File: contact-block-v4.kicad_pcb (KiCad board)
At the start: 2 copper layers, 42.5 x 19.2 mm, 10 parts, among them J1 629105136821, J2 M06SIP, J3 MPT2, U1 PIC16F1459-I_SS

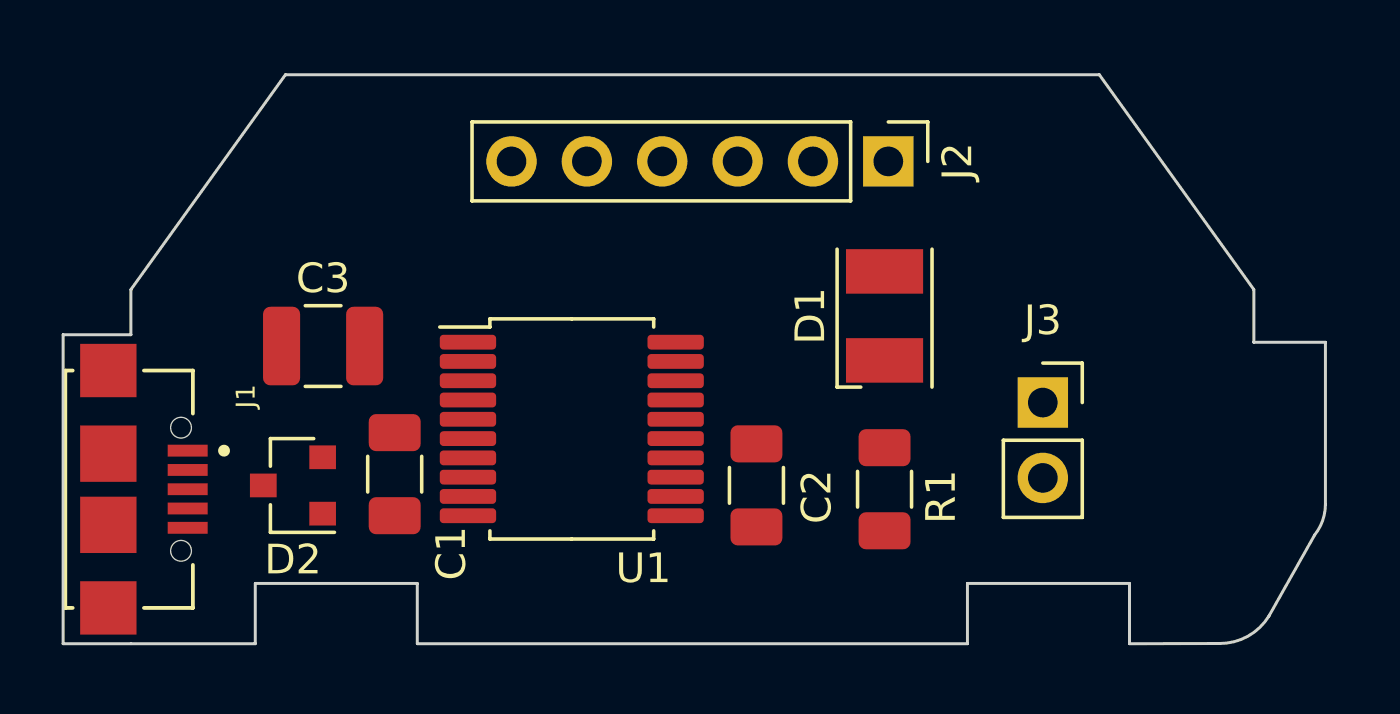
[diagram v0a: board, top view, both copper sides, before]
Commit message: Complete routing and add 3d models
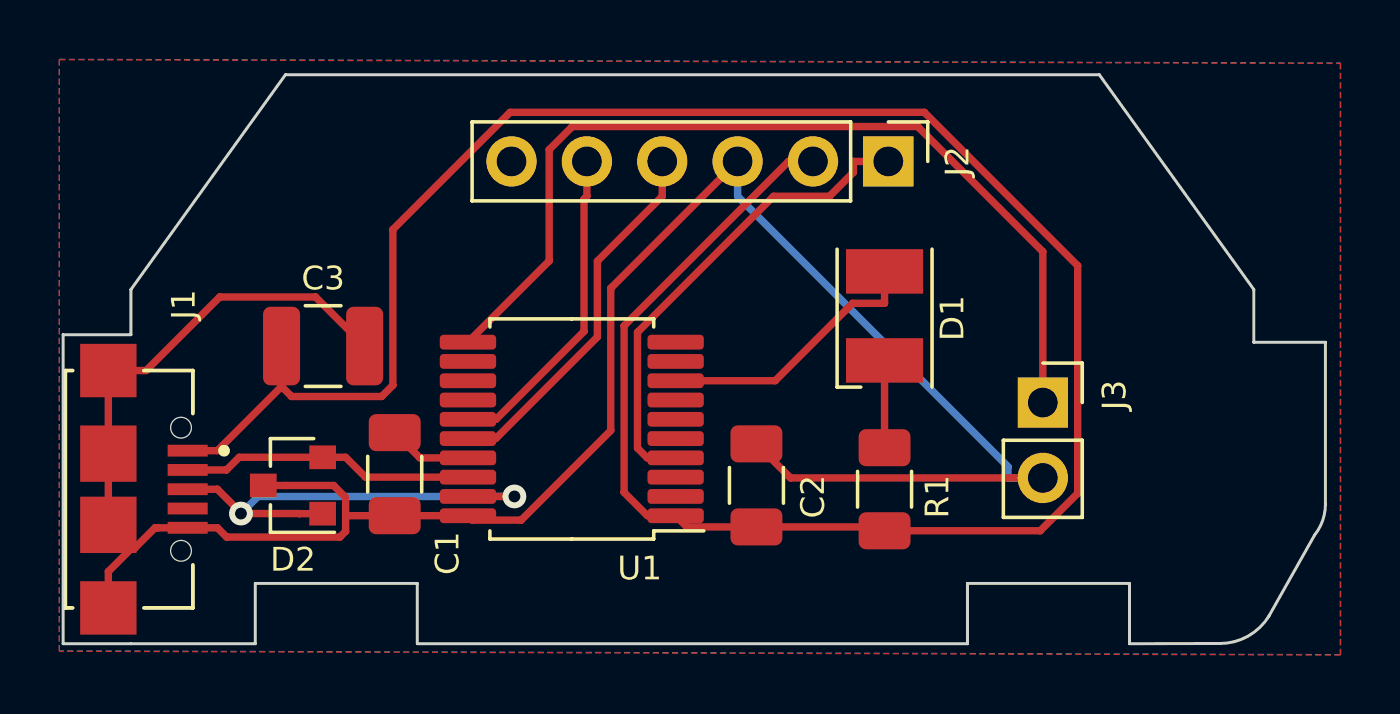
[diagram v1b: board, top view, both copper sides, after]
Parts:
- turned C1 to -90 degrees
- turned R1 to -90 degrees
- turned U1 to 180 degrees
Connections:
- D1 pad 1: (no net) -> Net-(D1-Pad1)
- D1 pad 2: (no net) -> Net-(D1-Pad2)
- J1 pad S1: (no net) -> GND
- J1 pad S2: (no net) -> GND
- J1 pad S3: (no net) -> GND
- J1 pad S4: (no net) -> GND
- R1 pad 1: Net-(D1-PadA) -> Net-(D1-Pad1)
- U1 pad 8: Net-(D1-PadC) -> Net-(D1-Pad2)
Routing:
- net +5V: track 0.00 -> 79.9 mm
- net GND: track 0.00 -> 77.6 mm
- net Net-(J3-Pad1): track 0.00 -> 31.4 mm
- net //MCLR: track 0.00 -> 16.4 mm
- net /D+: track 0.00 -> 15.9 mm, vias 0 -> 2
- net /PGD: track 0.00 -> 12.6 mm
- net /PGC: track 0.00 -> 10.9 mm
- net /D-: track 0.00 -> 9.90 mm
- net Net-(D1-Pad2): track 0.00 -> 9.20 mm
- net Net-(D1-Pad1): track 0.00 -> 2.94 mm
- net Net-(C1-Pad1): track 0.00 -> 2.82 mm
- added copper zone on B.Cu, net GND
- added copper zone on F.Cu, net GND

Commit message: Add doc images and bom
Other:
- board text added: "USB Big Red Button by Tisham Dhar Derived from work by @bikerglen v0.1 29/11/2020 http://whatnick.com OSHW TAPR"
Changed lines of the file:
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@@
     (pad "2" thru_hole oval (at 0 2.54) (size 1.7 1.7) (drill 1) (layers *.Cu *.Mask)
       (net 1 "GND") (pinfunction "1"))
-    (model "${KISYS3DMOD}/Connector_PinSocket_2.54mm.3dshapes/PinSocket_1x02_P2.54mm_Vertical.wrl"
+    (model "${KISYS3DMOD}/Connector_PinHeader_2.54mm.3dshapes/PinHeader_1x02_P2.54mm_Horizontal.step"
       (offset (xyz 0 0 0))
       (scale (xyz 1 1 1))
@@
   (gr_line (start 96.139 81.534) (end 96.139 91.948) (layer "Edge.Cuts") (width 0.1))
   (gr_line (start 138.322214 88.280371) (end 136.778999 91.017717) (layer "Edge.Cuts") (width 0.1))
+  (gr_text "USB Big Red Button\nby Tisham Dhar\nDerived from work by @bikerglen\nv0.1 29/11/2020\nhttp://whatnick.com\nOSHW TAPR" (at 117.602 82.042) (layer "B.SilkS")
+    (effects (font (size 1 1) (thickness 0.25)) (justify mirror))
+  )
   (segment (start 101.4179 80.2614) (end 98.9383 82.741) (width 0.25) (layer "F.Cu") (net 1))
   (segment (start 109.9316 87.7816) (end 111.5798 87.7816) (width 0.25) (layer "F.Cu") (net 1))
